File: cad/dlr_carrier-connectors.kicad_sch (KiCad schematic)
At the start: 5 parts, among them J11 DEBUG_UART, J12 USBC_COMMISSIONING, J3 BAT

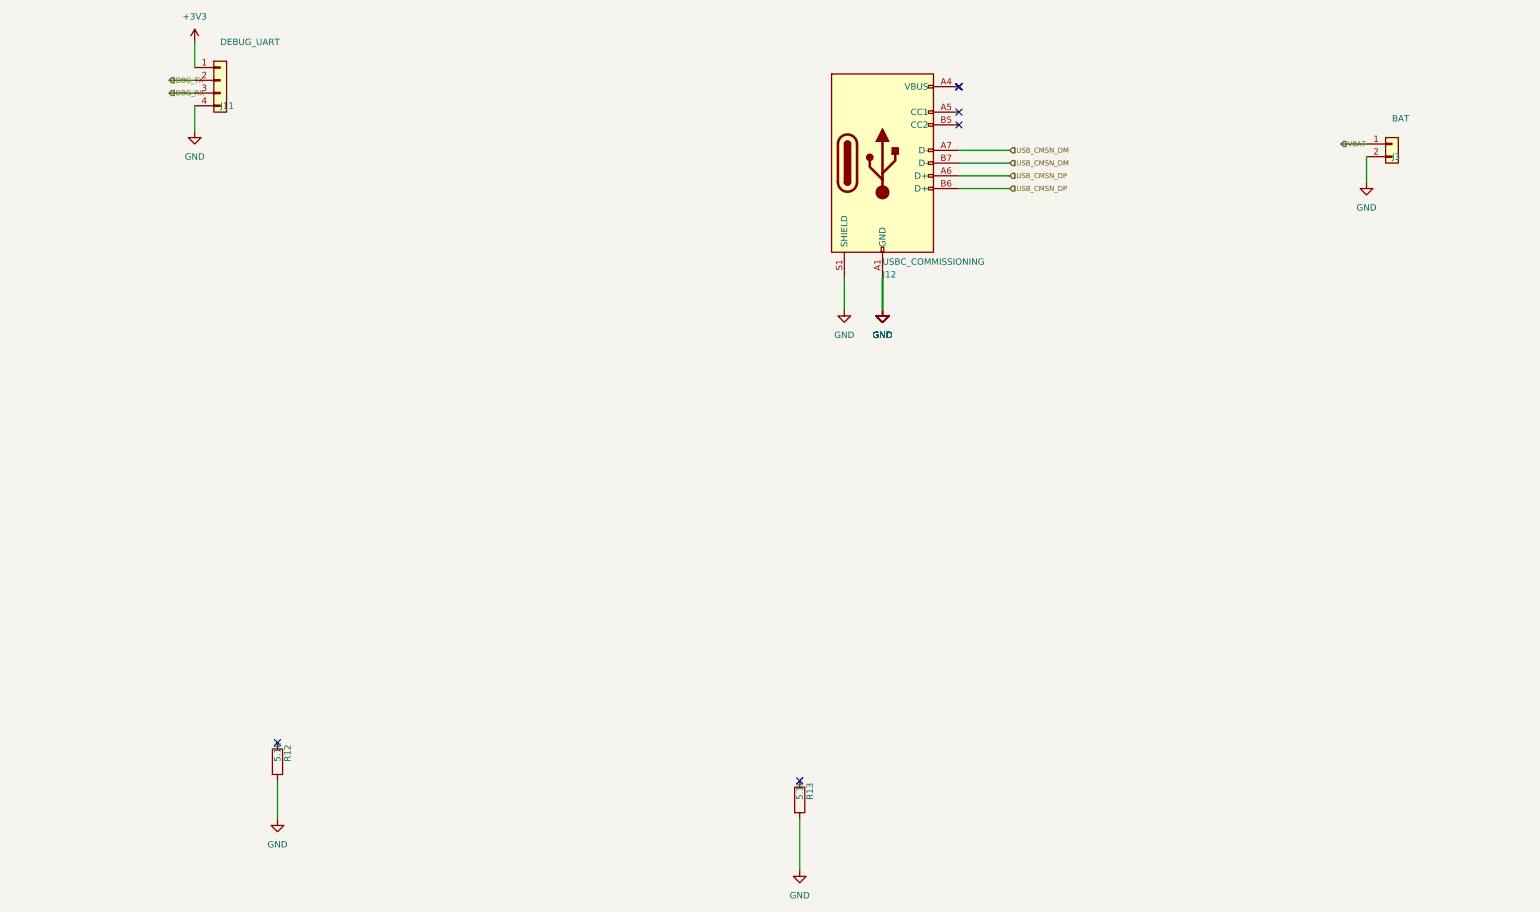
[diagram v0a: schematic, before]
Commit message: 🗺 feat(cad): scripted schematic + board pipeline, 4-layer stack
The committed board had almost every pad on +3V3 — no 5V_RAIL, VBAT or SDA1 net
existed on it at all — so the gerbers in output/ were never a valid board. Cause:
"Update PCB from Schematic" is GUI-only, so nothing kept the board honest, and the
schematic generator itself was merging nets.

Schematic generator:
  * power stubs now run along the pin direction; they used to be forced up or down
    regardless, which drove a 5V_RAIL stub straight through the buck inductor's
    BUCK_SW pin
  * PWR_FLAGs are placed by rule — any net that reaches a power-input pin with no
    power-output pin gets exactly one — instead of a hardcoded list, which is what
    the new VBAT and CHG_VCC rails needed
  * placement is deterministic; it used Python's salted hash(), so no two runs
    produced the same schematic
  * sch_guard fails the build on any cross-net wire/pin collision
  * ~700 lines of dead single-sheet generator removed
  ERC: 0 violations across all 8 sheets.

Board pipeline (cad/drawing/, all scripted, no GUI step):
  sync_pcb      rebuilds every footprint from the library and reassigns every pad
                net from the SKiDL netlist — the replacement for F8
  board_setup   4-layer SIG/GND/5V/SIG stack, rules, net classes, planes (ADR-016)
  route_pcb     DSN -> Freerouting -> SES, after patching the DSN so plane layers
                are "power" (the router was slicing the planes with signals) and
                the plane declarations are dropped (the router had been leaving
                GND and 5V pads with no path to the plane at all)
  stitch_planes vias from surface pads into their plane
  close_gaps    closes what the router leaves, using real segment-to-segment
                clearance; it never forces copper through another net

DRC: 265 unconnected -> 5, with no clearance, short, annular-ring or courtyard
errors. The remaining 5 are escapes on the DF40, the VQFN and the MSOP; they are
l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
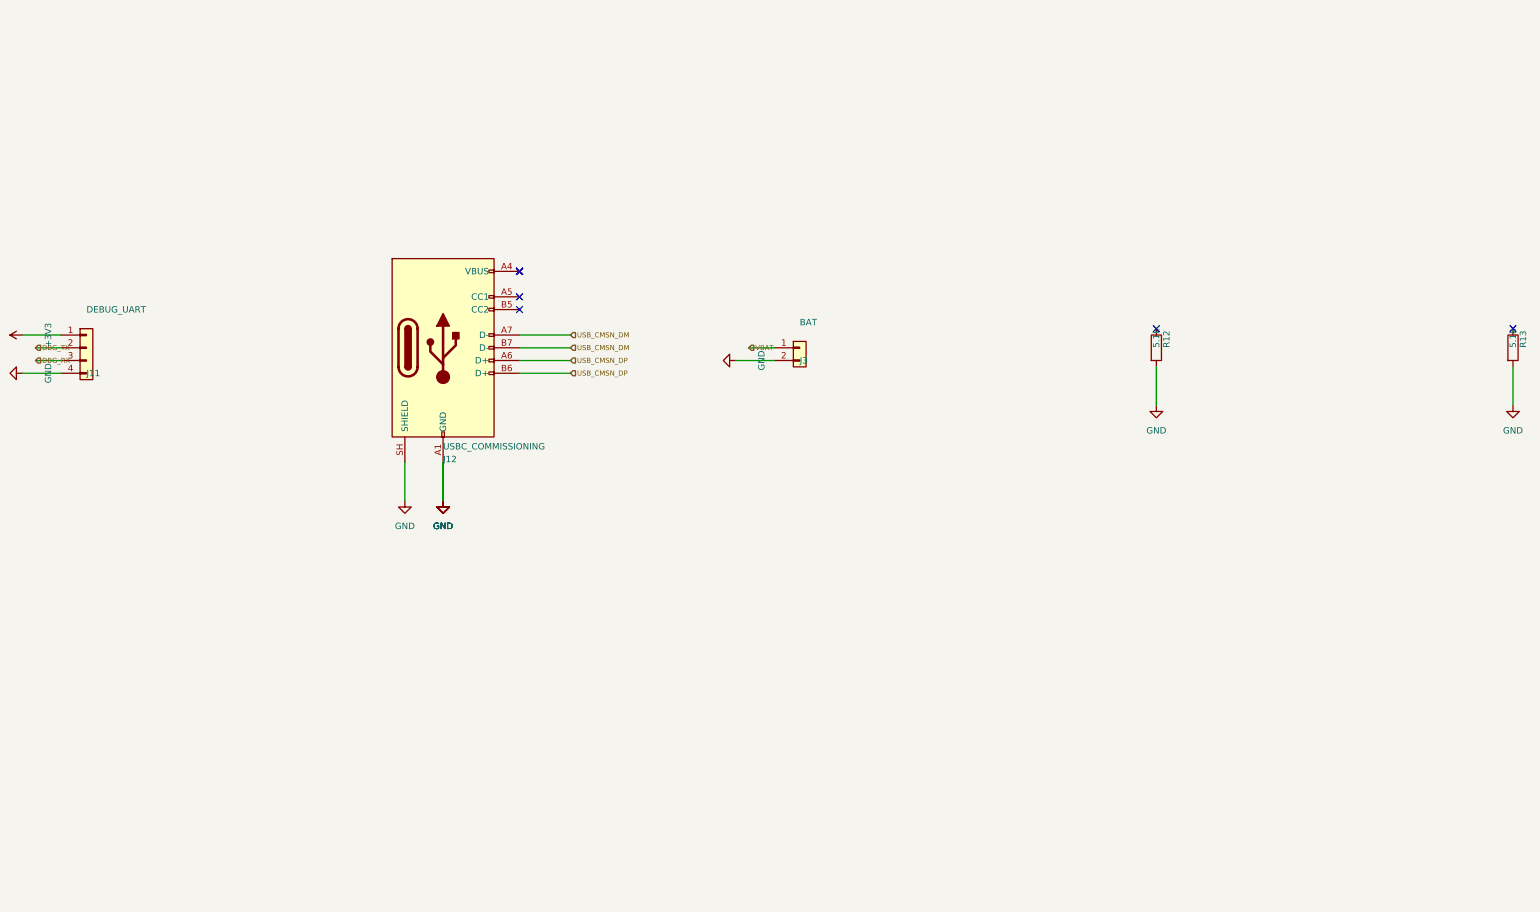
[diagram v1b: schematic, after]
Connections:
- net GND: now also J12.SH (SHIELD); no longer J12.S1 (SHIELD)

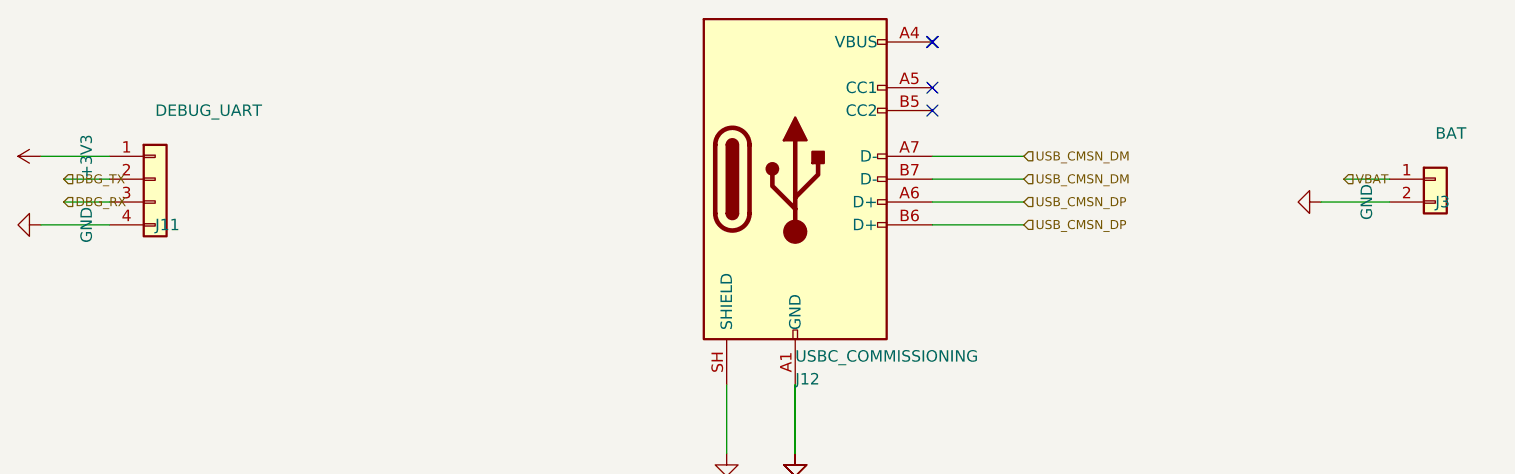
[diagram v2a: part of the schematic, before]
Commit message: 🩺 fix(schematic): match hierarchical label type to the sheet pin
The 117 KiCad 9 errors were a type mismatch, not the hierarchy metadata: every
child hierarchical label was written as `(shape input)` while the root's sheet pins
are bidirectional. KiCad's hier_label_mismatch check compares electrical type as
well as name, so on KiCad 9 every cross-sheet net failed, and the root labels then
read as dangling. KiCad 10 tolerates the mismatch, which is why it passed here.

kicad-sch-api 0.5.6 accepts a shape argument on add_hierarchical_label and ignores
it — the third serialization bug worked around in this generator — so the shape is
rewritten in the saved sheet.

Co-Authored-By: Claude Opus 5 <noreply@anthropic.com>
Claude-Session: https://claude.ai/code/session_011xr7VCL7rkJj2WE2uQF7sF
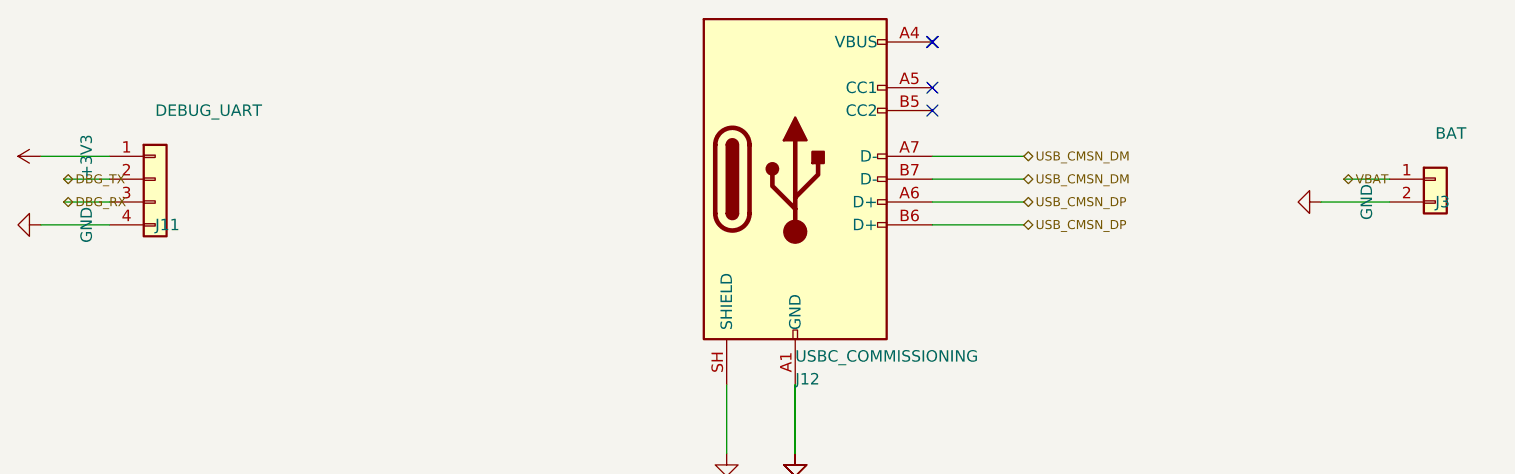
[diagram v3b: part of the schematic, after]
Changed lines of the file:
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@@
 		(instances
 			(project "CONNECTORS"
-				(path "/adebc692-74c5-4a96-a793-c959ba4a5cbc"
+				(path "/8192665d-bcfc-4432-b821-887d2ec6e9bf"
 					(reference "J11")
 					(unit 1)
@@
 		(instances
 			(project "CONNECTORS"
-				(path "/adebc692-74c5-4a96-a793-c959ba4a5cbc"
+				(path "/8192665d-bcfc-4432-b821-887d2ec6e9bf"
 					(reference "J12")
 					(unit 1)
@@
 		(instances
 			(project "CONNECTORS"
-				(path "/adebc692-74c5-4a96-a793-c959ba4a5cbc"
+				(path "/8192665d-bcfc-4432-b821-887d2ec6e9bf"
 					(reference "J3")
 					(unit 1)
@@
 		(instances
 			(project "CONNECTORS"
-				(path "/adebc692-74c5-4a96-a793-c959ba4a5cbc"
+				(path "/8192665d-bcfc-4432-b821-887d2ec6e9bf"
 					(reference "R12")
 					(unit 1)
@@
 		(instances
 			(project "CONNECTORS"
-				(path "/adebc692-74c5-4a96-a793-c959ba4a5cbc"
+				(path "/8192665d-bcfc-4432-b821-887d2ec6e9bf"
 					(reference "R13")
 					(unit 1)
@@
 		(instances
 			(project "CONNECTORS"
-				(path "/adebc692-74c5-4a96-a793-c959ba4a5cbc"
+				(path "/8192665d-bcfc-4432-b821-887d2ec6e9bf"
 					(reference "#PWR001")
 					(unit 1)
@@
 		(instances
 			(project "CONNECTORS"
-				(path "/adebc692-74c5-4a96-a793-c959ba4a5cbc"
+				(path "/8192665d-bcfc-4432-b821-887d2ec6e9bf"
 					(reference "#PWR002")
 					(unit 1)
@@
 		(instances
 			(project "CONNECTORS"
-				(path "/adebc692-74c5-4a96-a793-c959ba4a5cbc"
+				(path "/8192665d-bcfc-4432-b821-887d2ec6e9bf"
 					(reference "#PWR003")
 					(unit 1)
@@
 		(instances
 			(project "CONNECTORS"
-				(path "/adebc692-74c5-4a96-a793-c959ba4a5cbc"
+				(path "/8192665d-bcfc-4432-b821-887d2ec6e9bf"
 					(reference "#PWR004")
 					(unit 1)
@@
 		(instances
 			(project "CONNECTORS"
-				(path "/adebc692-74c5-4a96-a793-c959ba4a5cbc"
+				(path "/8192665d-bcfc-4432-b821-887d2ec6e9bf"
 					(reference "#PWR005")
 					(unit 1)
@@
 		(instances
 			(project "CONNECTORS"
-				(path "/adebc692-74c5-4a96-a793-c959ba4a5cbc"
+				(path "/8192665d-bcfc-4432-b821-887d2ec6e9bf"
 					(reference "#PWR006")
 					(unit 1)
@@
 		(instances
 			(project "CONNECTORS"
-				(path "/adebc692-74c5-4a96-a793-c959ba4a5cbc"
+				(path "/8192665d-bcfc-4432-b821-887d2ec6e9bf"
 					(reference "#PWR007")
 					(unit 1)
@@
 		(instances
 			(project "CONNECTORS"
-				(path "/adebc692-74c5-4a96-a793-c959ba4a5cbc"
+				(path "/8192665d-bcfc-4432-b821-887d2ec6e9bf"
 					(reference "#PWR008")
 					(unit 1)
@@
 		(instances
 			(project "CONNECTORS"
-				(path "/adebc692-74c5-4a96-a793-c959ba4a5cbc"
+				(path "/8192665d-bcfc-4432-b821-887d2ec6e9bf"
 					(reference "#PWR009")
 					(unit 1)
@@
 		(instances
 			(project "CONNECTORS"
-				(path "/adebc692-74c5-4a96-a793-c959ba4a5cbc"
+				(path "/8192665d-bcfc-4432-b821-887d2ec6e9bf"
 					(reference "#PWR010")
 					(unit 1)
@@
 	)
 	(hierarchical_label "DBG_RX"
-		(shape input)
+		(shape bidirectional)
 		(at 63.5 167.64 180)
 		(effects
@@
 	)
 	(hierarchical_label "DBG_TX"
-		(shape input)
+		(shape bidirectional)
 		(at 63.5 165.1 180)
 		(effects
@@
 	)
 	(hierarchical_label "USB_CMSN_DM"
-		(shape input)
+		(shape bidirectional)
 		(at 170.18 162.56 0)
 		(effects
@@
 	)
 	(hierarchical_label "USB_CMSN_DM"
-		(shape input)
+		(shape bidirectional)
 		(at 170.18 165.1 0)
 		(effects
@@
 	)
 	(hierarchical_label "USB_CMSN_DP"
-		(shape input)
+		(shape bidirectional)
 		(at 170.18 167.64 0)
 		(effects
@@
 	)
 	(hierarchical_label "USB_CMSN_DP"
-		(shape input)
+		(shape bidirectional)
 		(at 170.18 170.18 0)
 		(effects
@@
 	)
 	(hierarchical_label "VBAT"
-		(shape input)
+		(shape bidirectional)
 		(at 205.74 165.1 180)
 		(effects
@@
 	)
 	(sheet_instances
-		(path "/820a813e-d9a7-4e7e-a09b-b5e3c383add3"
+		(path "/8c69d83a-4880-48ed-90c2-e87a41cb06f9"
 			(page "7")
 		)
